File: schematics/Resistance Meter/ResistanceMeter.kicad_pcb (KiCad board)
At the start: 2 copper layers, 0 parts

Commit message: Design the PCB for the project
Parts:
- added D1: LED, LEDs:LED_D5.0mm_FlatTop, F.Cu at (196.8, 85.1)
- added D2: LED, LEDs:LED_D5.0mm_FlatTop, F.Cu at (196.8, 73.7)
- added D3: LED, LEDs:LED_D5.0mm_FlatTop, F.Cu at (196.8, 62.2)
- added D4: LED, LEDs:LED_D5.0mm_FlatTop, F.Cu at (186.7, 116.8)
- added D5: LED, LEDs:LED_D5.0mm_FlatTop, F.Cu at (199.4, 116.8)
- added D6: LED, LEDs:LED_D5.0mm_FlatTop, F.Cu at (196.8, 48.3)
- added J1: Conn_01x01_Female, Socket_Strips:Socket_Strip_Straight_1x01_Pitch2.54mm, F.Cu at (194.3, 100.3)
- added J2: Conn_01x01_Female, Socket_Strips:Socket_Strip_Straight_1x01_Pitch2.54mm, F.Cu at (201.9, 100.3)
- added J3: Conn_01x16_Female, Socket_Strips:Socket_Strip_Straight_1x16_Pitch2.54mm, F.Cu at (108.0, 114.3)
- added J4: Conn_01x08_Male, Pin_Headers:Pin_Header_Straight_1x08_Pitch2.54mm, F.Cu at (123.2, 47.0)
- added J5: Conn_01x06_Male, Pin_Headers:Pin_Header_Straight_1x06_Pitch2.54mm, F.Cu at (141.0, 47.0)
- added J6: Conn_01x10_Male, Pin_Headers:Pin_Header_Straight_1x10_Pitch2.54mm, F.Cu at (119.4, 95.2)
- added J7: Conn_01x08_Male, Pin_Headers:Pin_Header_Straight_1x08_Pitch2.54mm, F.Cu at (141.0, 95.2)
- added Q1: IRF540N, TO_SOT_Packages_THT:TO-220-3_Horizontal, F.Cu at (179.1, 50.8)
- added Q2: IRF540N, TO_SOT_Packages_THT:TO-220-3_Horizontal, F.Cu at (158.8, 68.6)
- added R1: 220, Resistors_THT:R_Axial_DIN0207_L6.3mm_D2.5mm_P7.62mm_Horizontal, F.Cu at (190.5, 81.3)
- added R10: 220, Resistors_THT:R_Axial_DIN0207_L6.3mm_D2.5mm_P7.62mm_Horizontal, F.Cu at (190.5, 110.5)
- added R11: 220, Resistors_THT:R_Axial_DIN0207_L6.3mm_D2.5mm_P7.62mm_Horizontal, F.Cu at (203.2, 110.5)
- added R2: 220, Resistors_THT:R_Axial_DIN0207_L6.3mm_D2.5mm_P7.62mm_Horizontal, F.Cu at (190.5, 69.8)
- added R3: 220, Resistors_THT:R_Axial_DIN0207_L6.3mm_D2.5mm_P7.62mm_Horizontal, F.Cu at (190.5, 58.4)
- added R4: 220, Resistors_THT:R_Axial_DIN0207_L6.3mm_D2.5mm_P7.62mm_Horizontal, F.Cu at (190.5, 44.5)
- added R5: 220, Resistors_THT:R_Axial_DIN0207_L6.3mm_D2.5mm_P7.62mm_Horizontal, F.Cu at (174.0, 86.4)
- added R6: 220, Resistors_THT:R_Axial_DIN0207_L6.3mm_D2.5mm_P7.62mm_Horizontal, F.Cu at (179.1, 86.4)
- added R7: 10k, Resistors_THT:R_Axial_DIN0207_L6.3mm_D2.5mm_P7.62mm_Horizontal, F.Cu at (166.4, 86.4)
- added R8: 10M, Resistors_THT:R_Axial_DIN0207_L6.3mm_D2.5mm_P7.62mm_Horizontal, F.Cu at (158.8, 86.4)
- added R9: 220, Resistors_THT:R_Axial_DIN0207_L6.3mm_D2.5mm_P7.62mm_Horizontal, F.Cu at (143.5, 106.7)
- added RV1: 10k, Potentiometers:Potentiometer_Trimmer_ACP_CA9v_Horizontal_Px10.0mm_Py5.0mm, F.Cu at (88.9, 108.0)
- added SW1: SW_Push, Buttons_Switches_THT:SW_PUSH_6mm_h4.3mm, F.Cu at (184.2, 134.6)
- added SW2: SW_Push, Buttons_Switches_THT:SW_PUSH_6mm_h4.3mm, F.Cu at (196.8, 134.6)
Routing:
- net +5V: track 0.00 -> 330.8 mm, vias 0 -> 3
- net Earth: track 0.00 -> 288.1 mm, vias 0 -> 1
- net /ANALOG_INPUT: track 0.00 -> 158.5 mm
- net /b3: track 0.00 -> 140.1 mm
- net /b6: track 0.00 -> 120.8 mm
- net /b2: track 0.00 -> 115.8 mm
- net /a14: track 0.00 -> 110.6 mm
- net /b4: track 0.00 -> 109.3 mm
- net /a13: track 0.00 -> 106.3 mm
- net /a12: track 0.00 -> 101.2 mm
- net /a11: track 0.00 -> 97.4 mm
- net /b5: track 0.00 -> 87.4 mm
- net Net-(Q1-Pad3): track 0.00 -> 40.6 mm
- net /a3: track 0.00 -> 23.1 mm
- net /a6: track 0.00 -> 22.7 mm
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- added copper zone on B.Cu, net Earth
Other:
- board outline added: 127 x 100.3 mm
- board text added: "16"
- board text added: "<-"
- board text added: "ARDUINO UNO"
- board text added: "Brightness"
- board text added: "Designed by Petar Nikolov"
- board text added: "HIGH"
- board text added: "LCD"
- board text added: "LOW"
- board text added: "MEASURE"
- board text added: "MEASURED RESISTANCE"
- board text added: "MID"
- board text added: "PWR"
- board text added: "RANGE"

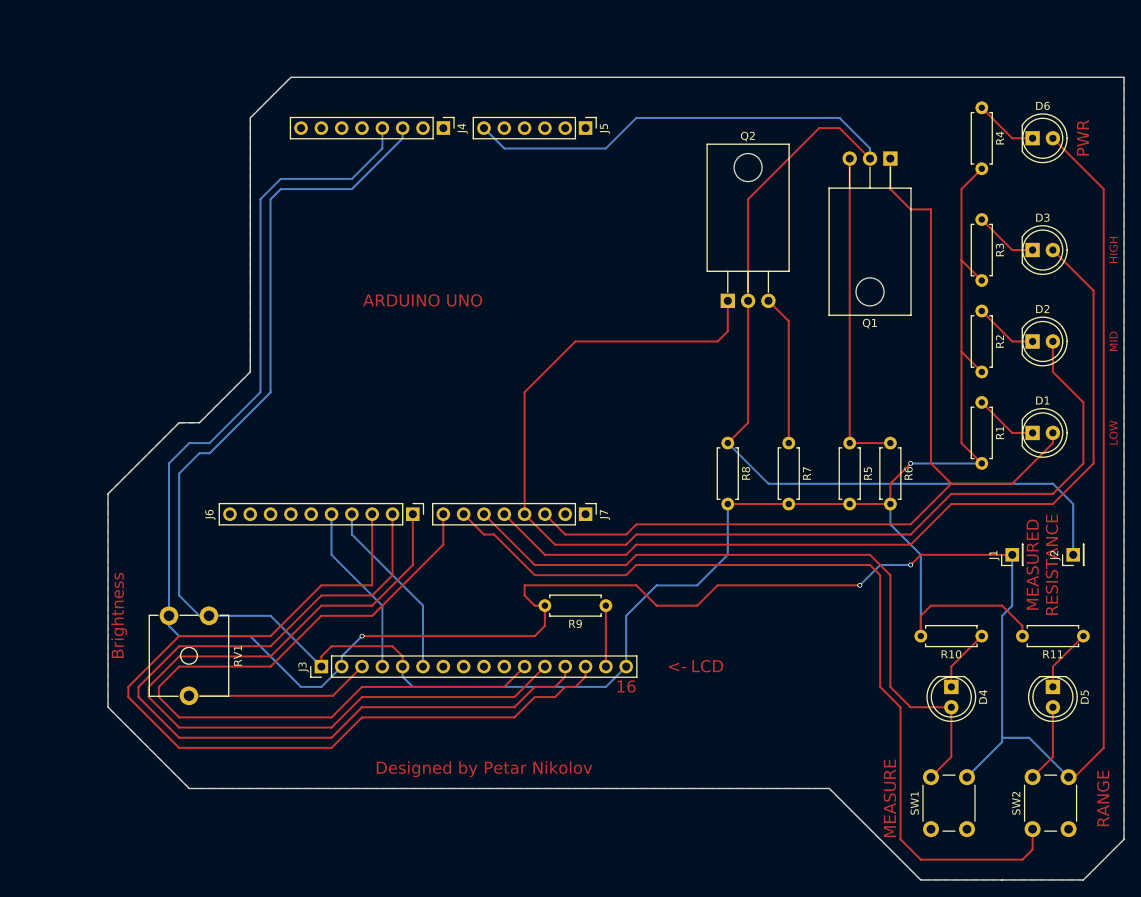
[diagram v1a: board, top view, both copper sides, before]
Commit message: Completely redo project PCB
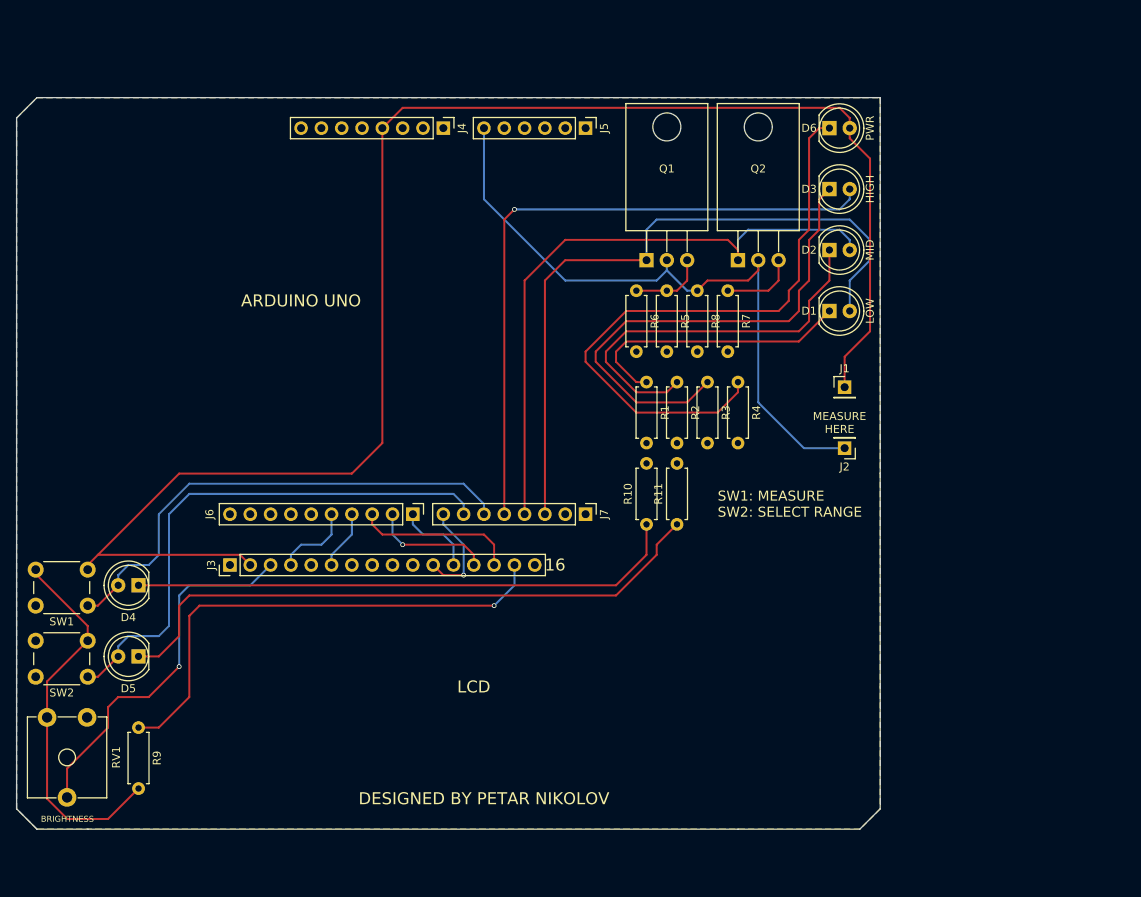
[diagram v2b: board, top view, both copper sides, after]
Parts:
- moved SW2 119.6 mm to (78.7, 115.6), turned to 180 degrees
- moved D5 114.4 mm to (85.1, 113.0), turned to 180 degrees
- moved SW1 109.1 mm to (78.7, 106.7), turned to 180 degrees
- moved D4 102.4 mm to (85.1, 104.1), turned to 180 degrees
- moved R9 60.4 mm to (85.1, 121.9), turned to 270 degrees
- moved R11 52.7 mm to (152.4, 96.5), turned to 90 degrees
- moved R4 45.9 mm to (160.0, 78.7)
- moved R10 44.2 mm to (148.6, 96.5), turned to 90 degrees
- moved R1 42.0 mm to (148.6, 78.7)
- moved R3 39.9 mm to (156.2, 78.7)
- moved R2 39.1 mm to (152.4, 78.7)
- moved R6 37.0 mm to (147.3, 67.3)
- moved Q1 33.0 mm to (148.6, 63.5), turned to 0 degrees
- moved J2 31.5 mm to (173.4, 87.0), turned to 180 degrees
- moved R5 29.8 mm to (151.1, 67.3)
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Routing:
- net Earth: track 288.1 -> 0.00 mm, vias 1 -> 0
- net /a12: track 101.2 -> 9.94 mm
- net /a13: track 106.3 -> 15.0 mm, vias 0 -> 1
- net /a14: track 110.6 -> 20.1 mm
- net /a11: track 97.4 -> 13.0 mm, vias 0 -> 1
- net +5V: track 330.8 -> 246.9 mm, vias 3 -> 0
- net /ANALOG_INPUT: track 158.5 -> 83.5 mm
- net Net-(D6-Pad1): track 7.93 -> 77.7 mm
- net Net-(D5-Pad1): track 7.93 -> 77.1 mm
- net /b3: track 140.1 -> 78.6 mm
- net Net-(D4-Pad1): track 7.93 -> 68.9 mm
- net /a15: track 7.62 -> 62.8 mm, vias 0 -> 1
- net Net-(D3-Pad1): track 7.93 -> 62.7 mm
- net /b6: track 120.8 -> 67.2 mm
- net Net-(D2-Pad1): track 7.93 -> 49.2 mm
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- added copper zone on F.Cu, net Earth
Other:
- board size 127 x 100.3 mm -> 108 x 91.4 mm
- board text added: "BRIGHTNESS"
- board text added: "DESIGNED BY PETAR NIKOLOV"
- board text added: "MEASURE HERE"
- board text added: "SW1: MEASURE SW2: SELECT RANGE"
- board text removed: "<-"
- board text removed: "Brightness"
- board text removed: "Designed by Petar Nikolov"
- board text removed: "MEASURE"
- board text removed: "MEASURED RESISTANCE"
- board text removed: "RANGE"

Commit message: Revise the PCB layout (again)
Also, changed a few of the design's footprints.
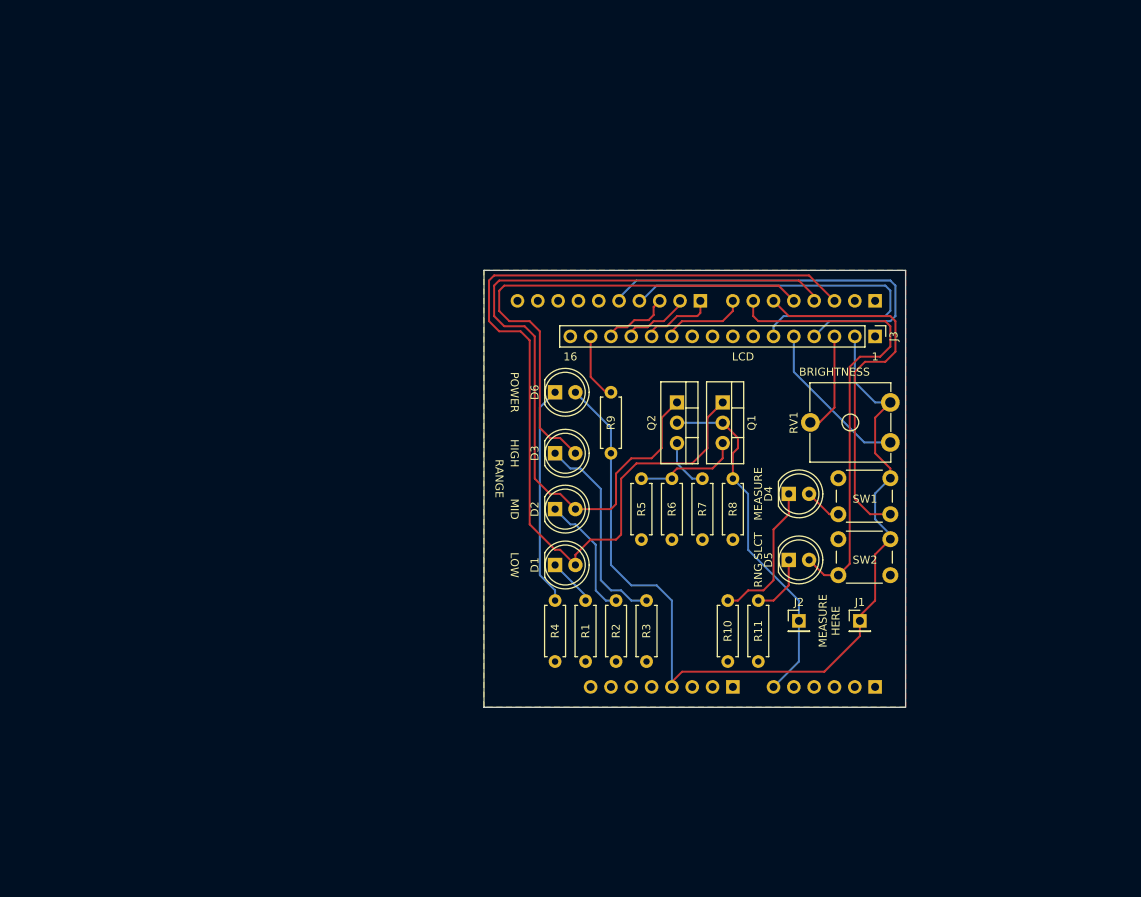
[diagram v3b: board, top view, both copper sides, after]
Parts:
- D1, D2, D3, D4, D5, D6: footprint LEDs:LED_D5.0mm_FlatTop -> LEDs:LED_D5.0mm
- J4, J5, J6, J7: moved to B.Cu
- Q1, Q2: footprint TO_SOT_Packages_THT:TO-220-3_Horizontal -> TO_SOT_Packages_THT:TO-220-3_Vertical
- moved RV1 112.5 mm to (179.1, 81.3), turned to 180 degrees
- moved SW2 101.1 mm to (179.1, 102.9)
- moved SW1 101.0 mm to (179.1, 95.2)
- moved J3 85.6 mm to (177.2, 73.0), turned to 270 degrees
- moved D5 82.2 mm to (166.4, 101.0), turned to 0 degrees
- moved D4 82.1 mm to (166.4, 92.7), turned to 0 degrees
- moved J4 78.7 mm to (159.4, 116.8), turned to 90 degrees
- moved J5 78.7 mm to (177.2, 116.8), turned to 90 degrees
- moved R9 72.4 mm to (144.1, 80.0)
- moved D6 47.6 mm to (137.2, 80.0)
- moved D3 47.6 mm to (137.2, 87.6)
- moved D2 47.2 mm to (137.2, 94.6)
- moved D1 46.7 mm to (137.2, 101.6)
- moved J7 45.0 mm to (177.2, 68.6), turned to 90 degrees
- moved J6 44.8 mm to (155.3, 68.6), turned to 90 degrees
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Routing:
- net +5V: track 246.9 -> 115.3 mm
- net Net-(D5-Pad1): track 77.1 -> 7.77 mm
- net /a15: track 62.8 -> 8.41 mm, vias 1 -> 0
- net Net-(D4-Pad1): track 68.9 -> 18.4 mm
- net Net-(D6-Pad1): track 77.7 -> 27.6 mm
- net /a6: track 7.40 -> 51.6 mm
- net /a4: track 9.94 -> 51.1 mm
- net /ANALOG_INPUT: track 83.5 -> 44.5 mm
- net Net-(D3-Pad1): track 62.7 -> 25.8 mm
- net /b2: track 86.2 -> 120.6 mm
- net /a3: track 46.3 -> 12.7 mm, vias 1 -> 0
- net Net-(D2-Pad1): track 49.2 -> 15.7 mm
- net Net-(D1-Pad1): track 34.9 -> 6.02 mm
- net Earth: track 0.00 -> 20.2 mm
- net /b3: track 78.6 -> 98.8 mm
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- removed copper zone on B.Cu, net Earth
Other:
- board size 108 x 91.4 mm -> 52.7 x 54.6 mm
- board text added: "1"
- board text added: "MEASURE"
- board text added: "POWER"
- board text added: "RANGE"
- board text added: "RNG SLCT"
- board text removed: "ARDUINO UNO"
- board text removed: "PWR"
- board text removed: "SW1: MEASURE SW2: SELECT RANGE"
